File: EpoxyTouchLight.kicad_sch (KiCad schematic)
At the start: 22 parts, among them J1 Serial, SW1 SW_DPDT_x2, SW2 Button, U1 ESP32-WROOM-32

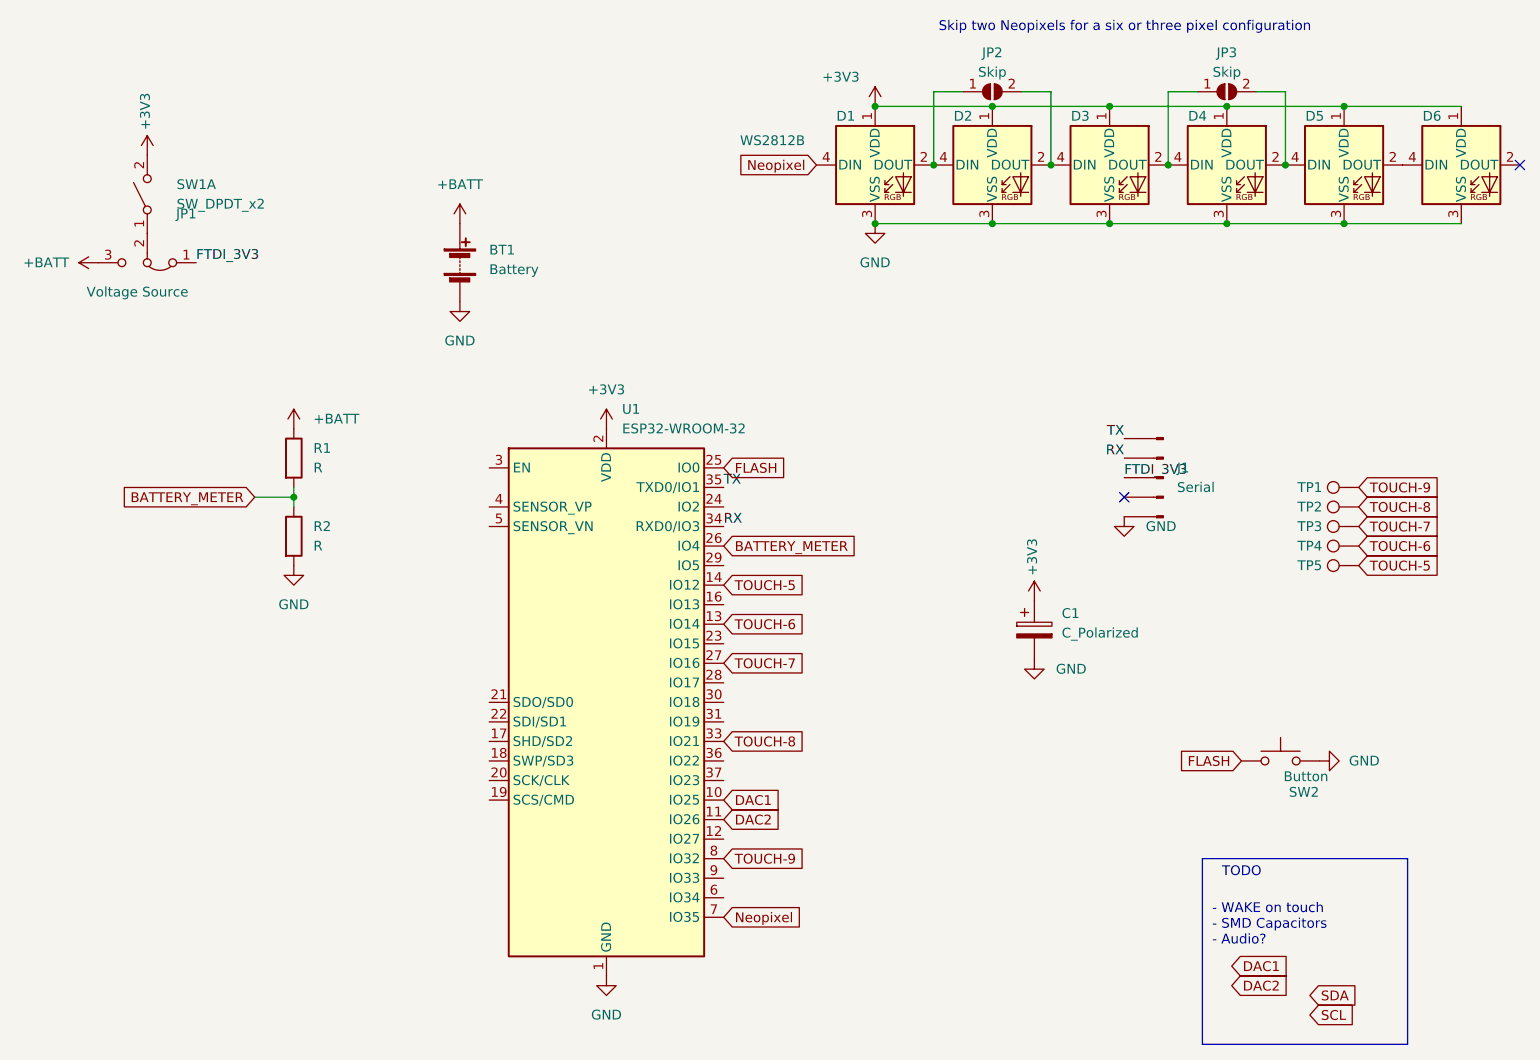
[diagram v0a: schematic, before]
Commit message: Add radio receiver module
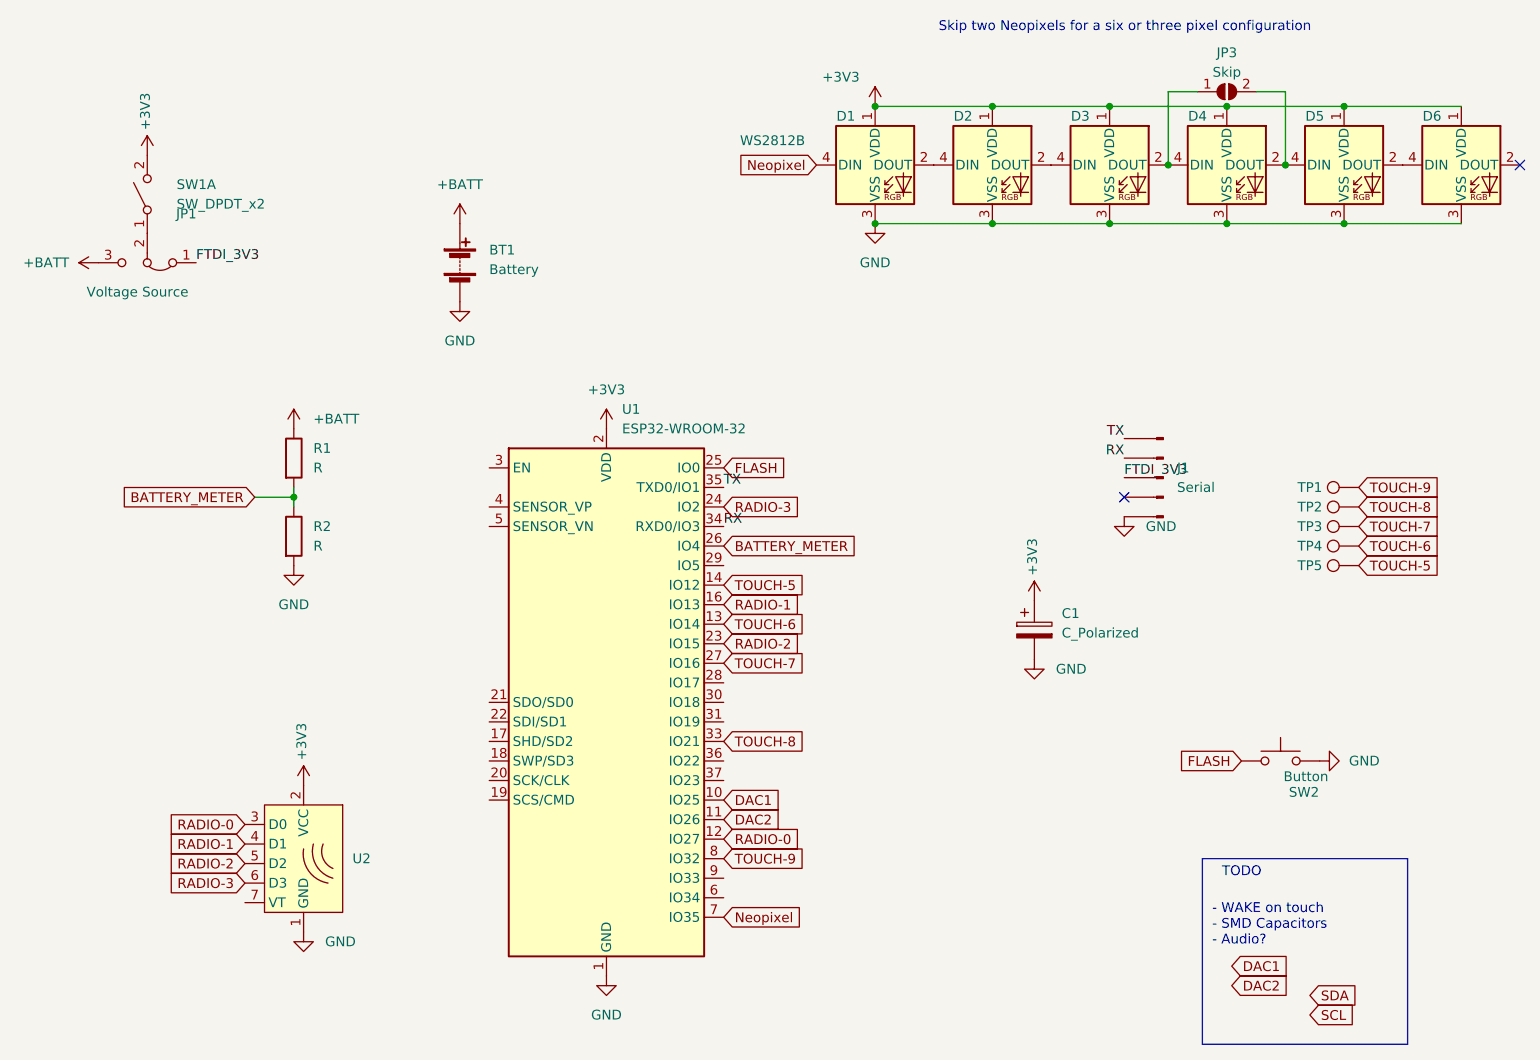
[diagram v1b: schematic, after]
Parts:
- removed JP2: Skip, Jumper:SolderJumper-2_P1.3mm_Open_TrianglePad1.0x1.5mm, symbol Jumper:SolderJumper_2_Open
- added U2: radio-receiver, radio-receiver:radio-receiver, symbol radio-receiver:radio-receiver
- J1: footprint Connector_PinHeader_2.54mm:PinHeader_1x05_P2.54mm_Vertical -> Connector_PinHeader_2.54mm:PinHeader_1x05_P2.54mm_Horizontal
- JP1: footprint Connector_PinHeader_2.54mm:PinHeader_1x03_P2.54mm_Vertical -> Connector_PinHeader_2.54mm:PinHeader_1x03_P2.54mm_Horizontal
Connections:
- net +3V3: now also U2.2 (VCC)
- net GND: now also U2.1 (GND)
- net RADIO-0: now reaches U1.12 (IO27)
- net RADIO-0: now also U2.3 (D0)
- net RADIO-1: now reaches U1.16 (IO13)
- net RADIO-1: now also U2.4 (D1)
- net RADIO-2: now reaches U1.23 (IO15)
- net RADIO-2: now also U2.5 (D2)
- net RADIO-3: now reaches U1.24 (IO2)
- net RADIO-3: now also U2.6 (D3)
